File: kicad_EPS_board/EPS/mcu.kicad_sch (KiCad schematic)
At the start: 25 parts, among them P1 CONN_01X02, U1 24AA32, U2 STM32L452CCU6, U3 TCAN334, Y1 8MHz

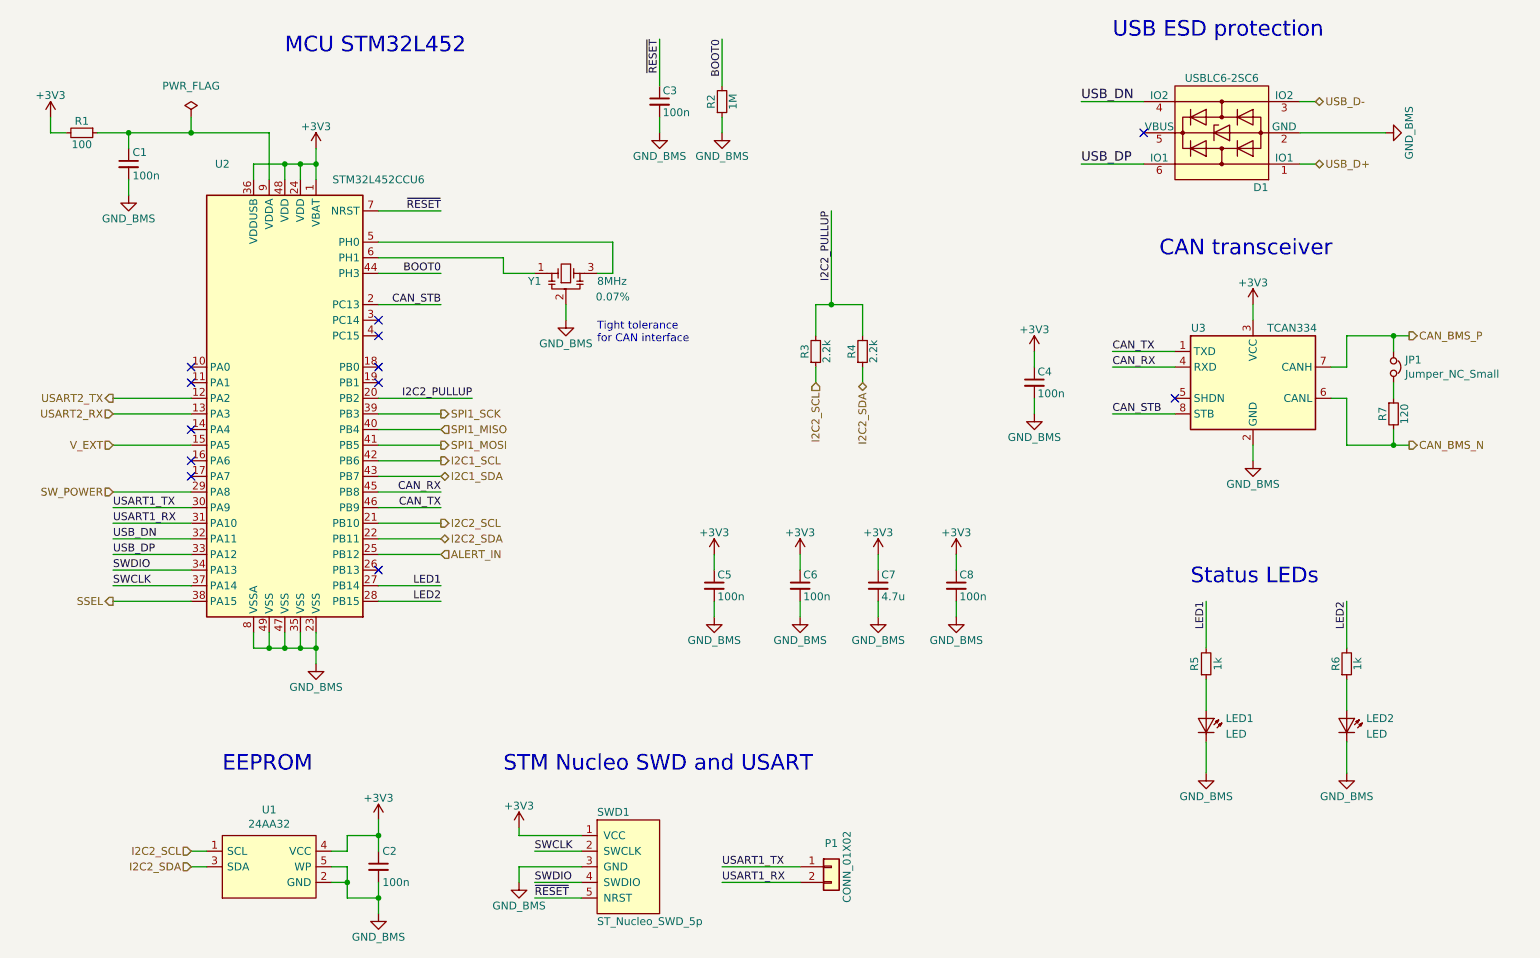
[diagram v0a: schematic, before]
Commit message: kicad EPS board V2 revision and already generated html doc files
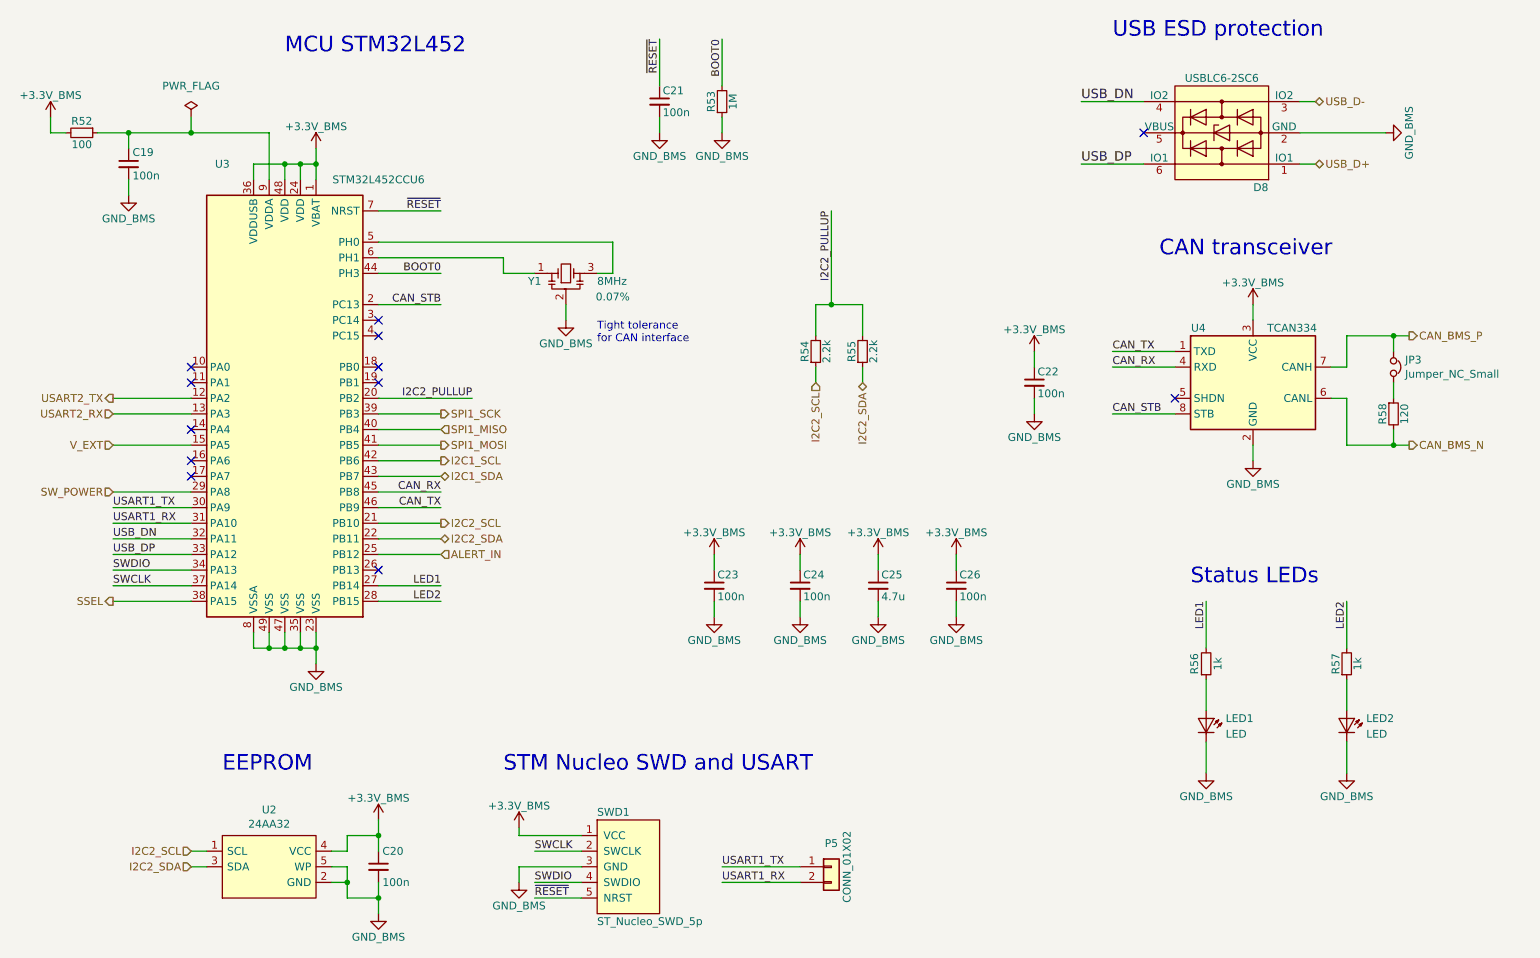
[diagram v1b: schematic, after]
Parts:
- renumbered C1 to C19, C2 to C20, C3 to C21, C4 to C22, C5 to C23, C6 to C24, C7 to C25, C8 to C26, D1 to D8, JP1 to JP3, P1 to P5, R1 to R52, R2 to R53, R3 to R54, R4 to R55, R5 to R56, R6 to R57, R7 to R58, U1 to U2, U2 to U3, U3 to U4
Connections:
- net +3V3 renamed +3.3V_BMS
